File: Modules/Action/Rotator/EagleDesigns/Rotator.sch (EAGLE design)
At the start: 9 parts, among them U2 ATMEGA328P_TQFP

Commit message: Revert "Merge branch 'version-1.2'"
This reverts commit 982d9c85d5bd00c48b539e840003de48d3cf178d, reversing
changes made to b3895ae538c161df72313035d3e956c7a5ec4dbc.
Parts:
- removed C1, C2: 22pF, adafruit:C-USC0603
- removed R2: 10K, resistor:R-US_R0603
- removed U$2: NX503, MakerWear:NX503
- removed U2: ATMEGA328P_TQFP, SparkFun-DigitalIC:ATMEGA328P_TQFP
- added U1: TINY85-20-DIP, SparkFun-DigitalIC:ATTINY45TINY85-20-DIP
- JP2: device SparkFun-Connectors:M03PTH -> SparkFun-Connectors:M04PTH
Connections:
- removed net 1X3SIN: U2.PC0(ADC0)
- removed net N$1: C1.1, U$2.P$1, U2.PB6(XTAL1/TOSC1)
- removed net N$3: C2.1, U$2.P$2, U2.PB7(XTAL2/TOSC2)
- removed net RESET: JP2.1, R2.1, U2.PC6(/RESET)
- removed net RX: JP2.2, U2.PD0(RXD)
- removed net TX: JP2.3, U2.PD1(TXD)
- new net MOSI: JP2.2, U1.PB0(MOSI)
- new net NRES: JP2.1, U1.PB5(NRES)
- new net OUT(MISO): JP2.3, JP3.1, U1.PB1(MISO)
- new net SCK: JP2.4, U1.PB2(SCK/ADC1)
- net 1X3SIN-SOUT: now also U1.PB3(ADC3)
- net GND: now also U1.GND; no longer C1.2, C2.2, U2.AGND, U2.GND@3, U2.GND@5
- net VCC: now also U1.VCC; no longer R2.2, U2.AVCC, U2.VCC@4, U2.VCC@6
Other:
- moved on the sheet: JP1, JP3, R1

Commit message: added Rotator #30 eagle files
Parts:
- removed U1: TINY85-20-DIP, SparkFun-DigitalIC:ATTINY45TINY85-20-DIP
- added C1, C2: 22pF, adafruit:C-USC0603
- added R2: 10K, resistor:R-US_R0603
- added U$2: NX503, MakerWear:NX503
- added U2: ATMEGA328P_TQFP, SparkFun-DigitalIC:ATMEGA328P_TQFP
- JP2: device SparkFun-Connectors:M04PTH -> SparkFun-Connectors:M03PTH
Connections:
- removed net MOSI: JP2.2, U1.PB0(MOSI)
- removed net NRES: JP2.1, U1.PB5(NRES)
- removed net OUT(MISO): JP2.3, JP3.1, U1.PB1(MISO)
- removed net SCK: JP2.4, U1.PB2(SCK/ADC1)
- new net 1X3SIN: U2.PC0(ADC0)
- new net N$1: C1.1, U$2.P$1, U2.PB6(XTAL1/TOSC1)
- new net N$3: C2.1, U$2.P$2, U2.PB7(XTAL2/TOSC2)
- new net RESET: JP2.1, R2.1, U2.PC6(/RESET)
- new net RX: JP2.2, U2.PD0(RXD)
- new net TX: JP2.3, U2.PD1(TXD)
- net 1X3SIN-SOUT: no longer U1.PB3(ADC3)
- net GND: now also C1.2, C2.2, U2.AGND, U2.GND@3, U2.GND@5; no longer U1.GND
- net VCC: now also R2.2, U2.AVCC, U2.VCC@4, U2.VCC@6; no longer U1.VCC
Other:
- moved on the sheet: JP1, JP3, R1

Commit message: fixed eagle files for new modules
SIN/SOUT was not correctly connected in them.
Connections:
- removed net 1X3SIN: U2.PC0(ADC0)
- new net SERVO: JP3.1, U2.PB1(OC1A)
- net 1X3SIN-SOUT: now also U2.PC0(ADC0)
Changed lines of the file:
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@@
 <pinref part="R1" gate="G$1" pin="2"/>
+</segment>
+<segment>
+<pinref part="U2" gate="U$1" pin="PC0(ADC0)"/>
+<wire x1="208.28" y1="55.88" x2="228.6" y2="55.88" width="0.1524" layer="91"/>
+<junction x="228.6" y="55.88"/>
+<label x="210.82" y="55.88" size="1.778" layer="95"/>
 </segment>
 </net>
@@
 </segment>
 </net>
-<net name="1X3SIN" class="0">
-<segment>
-<pinref part="U2" gate="U$1" pin="PC0(ADC0)"/>
-<wire x1="208.28" y1="55.88" x2="220.98" y2="55.88" width="0.1524" layer="91"/>
-<junction x="220.98" y="55.88"/>
-<label x="210.82" y="55.88" size="1.778" layer="95"/>
-</segment>
-</net>
 <net name="N$1" class="0">
 <segment>
@@
 </segment>
 </net>
+<net name="SERVO" class="0">
+<segment>
+<pinref part="U2" gate="U$1" pin="PB1(OC1A)"/>
+<wire x1="208.28" y1="7.62" x2="220.98" y2="7.62" width="0.1524" layer="91"/>
+<junction x="220.98" y="7.62"/>
+<label x="210.82" y="7.62" size="1.778" layer="95"/>
+</segment>
+<segment>
+<pinref part="JP3" gate="G$1" pin="1"/>
+<wire x1="302.26" y1="30.48" x2="284.48" y2="30.48" width="0.1524" layer="91"/>
+<junction x="284.48" y="30.48"/>
+<label x="287.02" y="30.48" size="1.778" layer="95"/>
+</segment>
+</net>

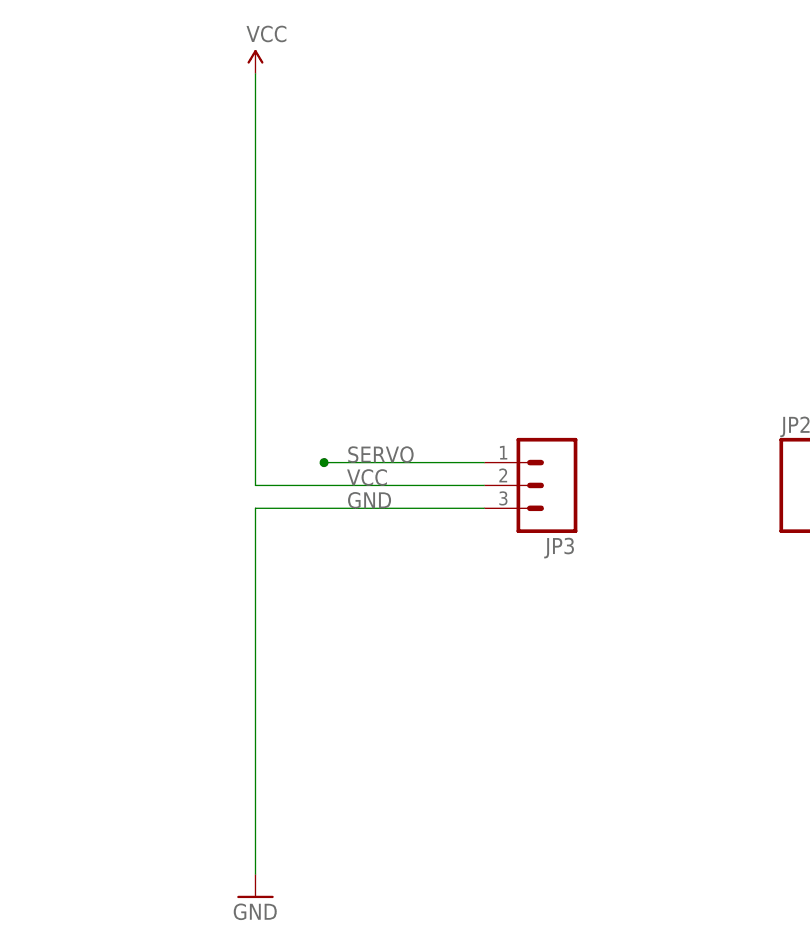
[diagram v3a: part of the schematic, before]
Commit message: Rotator: added final PCB #30
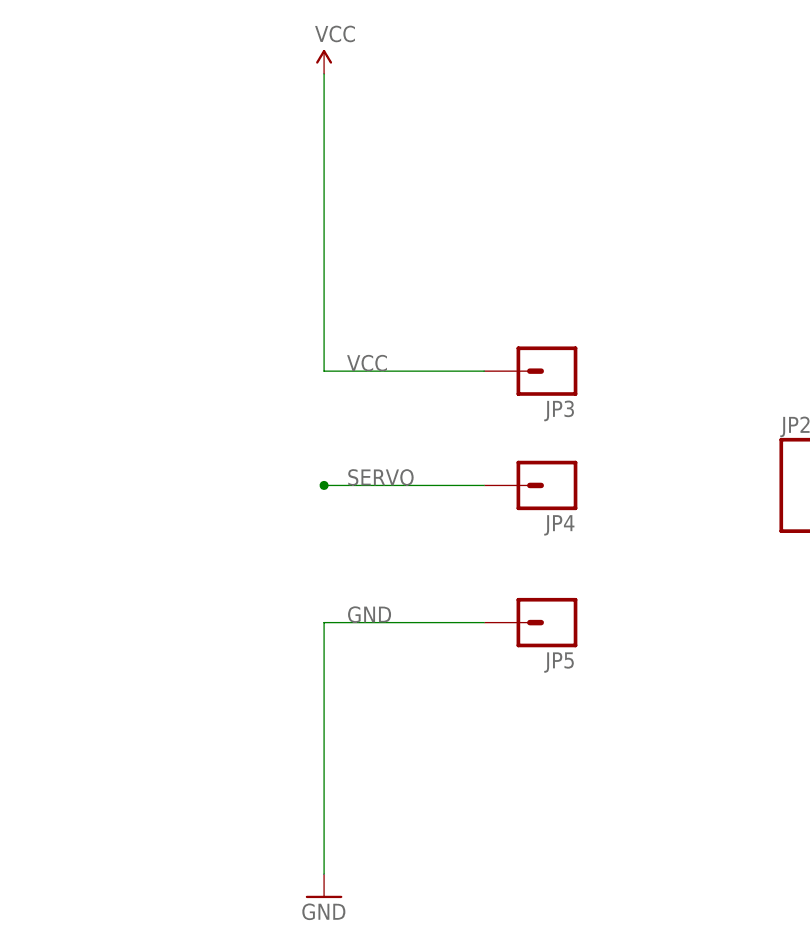
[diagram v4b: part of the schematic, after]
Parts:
- added JP4, JP5: (no value), SparkFun-Connectors:M01PTH
- JP3: device SparkFun-Connectors:M03PTH -> SparkFun-Connectors:M01PTH
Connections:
- net GND: now also JP5.1; no longer JP3.3
- net SERVO: now also JP4.1; no longer JP3.1
- net VCC: now also JP3.1; no longer JP3.2
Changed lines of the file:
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@@
 <part name="GND5" library="SparkFun-Aesthetics" deviceset="GND" device=""/>
 <part name="R1" library="adafruit" deviceset="R-US_" device="R0603" value="1M"/>
-<part name="JP3" library="SparkFun-Connectors" deviceset="M03" device="PTH"/>
 <part name="SUPPLY3" library="SparkFun-Aesthetics" deviceset="VCC" device=""/>
 <part name="GND3" library="SparkFun-Aesthetics" deviceset="GND" device=""/>
@@
 <part name="C1" library="adafruit" deviceset="C-US" device="C0603" value="22pF"/>
 <part name="C2" library="adafruit" deviceset="C-US" device="C0603" value="22pF"/>
+<part name="JP3" library="SparkFun-Connectors" deviceset="M01" device="PTH"/>
+<part name="JP4" library="SparkFun-Connectors" deviceset="M01" device="PTH"/>
+<part name="JP5" library="SparkFun-Connectors" deviceset="M01" device="PTH"/>
 </parts>
 <sheets>
@@
 <instance part="GND5" gate="1" x="58.42" y="-17.78"/>
 <instance part="R1" gate="G$1" x="58.42" y="15.24" rot="R90"/>
-<instance part="JP3" gate="G$1" x="309.88" y="27.94" rot="R180"/>
-<instance part="SUPPLY3" gate="G$1" x="276.86" y="73.66"/>
-<instance part="GND3" gate="1" x="276.86" y="-17.78"/>
+<instance part="SUPPLY3" gate="G$1" x="284.48" y="73.66"/>
+<instance part="GND3" gate="1" x="284.48" y="-17.78"/>
 <instance part="JP2" gate="G$1" x="337.82" y="27.94"/>
 <instance part="U2" gate="U$1" x="185.42" y="25.4"/>
@@
 <instance part="C1" gate="G$1" x="96.52" y="-10.16"/>
 <instance part="C2" gate="G$1" x="121.92" y="-10.16"/>
+<instance part="JP3" gate="G$1" x="309.88" y="40.64" rot="R180"/>
+<instance part="JP4" gate="G$1" x="309.88" y="27.94" rot="R180"/>
+<instance part="JP5" gate="G$1" x="309.88" y="12.7" rot="R180"/>
 </instances>
 <busses>
@@
 </segment>
 <segment>
-<pinref part="JP3" gate="G$1" pin="2"/>
-<wire x1="302.26" y1="27.94" x2="276.86" y2="27.94" width="0.1524" layer="91"/>
-<wire x1="276.86" y1="27.94" x2="276.86" y2="73.66" width="0.1524" layer="91"/>
 <pinref part="SUPPLY3" gate="G$1" pin="VCC"/>
-<label x="287.02" y="27.94" size="1.778" layer="95"/>
+<pinref part="JP3" gate="G$1" pin="1"/>
+<wire x1="284.48" y1="40.64" x2="284.48" y2="73.66" width="0.1524" layer="91"/>
+<wire x1="302.26" y1="40.64" x2="284.48" y2="40.64" width="0.1524" layer="91"/>
+<label x="287.02" y="40.64" size="1.778" layer="95"/>
 </segment>
 <segment>
@@
 </segment>
 <segment>
-<pinref part="JP3" gate="G$1" pin="3"/>
-<wire x1="302.26" y1="25.4" x2="276.86" y2="25.4" width="0.1524" layer="91"/>
-<wire x1="276.86" y1="25.4" x2="276.86" y2="-15.24" width="0.1524" layer="91"/>
+<wire x1="284.48" y1="12.7" x2="284.48" y2="-15.24" width="0.1524" layer="91"/>
 <pinref part="GND3" gate="1" pin="GND"/>
-<label x="287.02" y="25.4" size="1.778" layer="95"/>
+<pinref part="JP5" gate="G$1" pin="1"/>
+<wire x1="302.26" y1="12.7" x2="284.48" y2="12.7" width="0.1524" layer="91"/>
+<label x="287.02" y="12.7" size="1.778" layer="95"/>
 </segment>
 <segment>
@@
 <net name="SERVO" class="0">
 <segment>
+<pinref part="JP4" gate="G$1" pin="1"/>
+<wire x1="302.26" y1="27.94" x2="284.48" y2="27.94" width="0.1524" layer="91"/>
+<junction x="284.48" y="27.94"/>
+<label x="287.02" y="27.94" size="1.778" layer="95"/>
+</segment>
+<segment>
 <pinref part="U2" gate="U$1" pin="PB1(OC1A)"/>
 <wire x1="208.28" y1="7.62" x2="220.98" y2="7.62" width="0.1524" layer="91"/>
@@
 <label x="210.82" y="7.62" size="1.778" layer="95"/>
 </segment>
-<segment>
-<pinref part="JP3" gate="G$1" pin="1"/>
-<wire x1="302.26" y1="30.48" x2="284.48" y2="30.48" width="0.1524" layer="91"/>
-<junction x="284.48" y="30.48"/>
-<label x="287.02" y="30.48" size="1.778" layer="95"/>
-</segment>
-</net>
+</net>

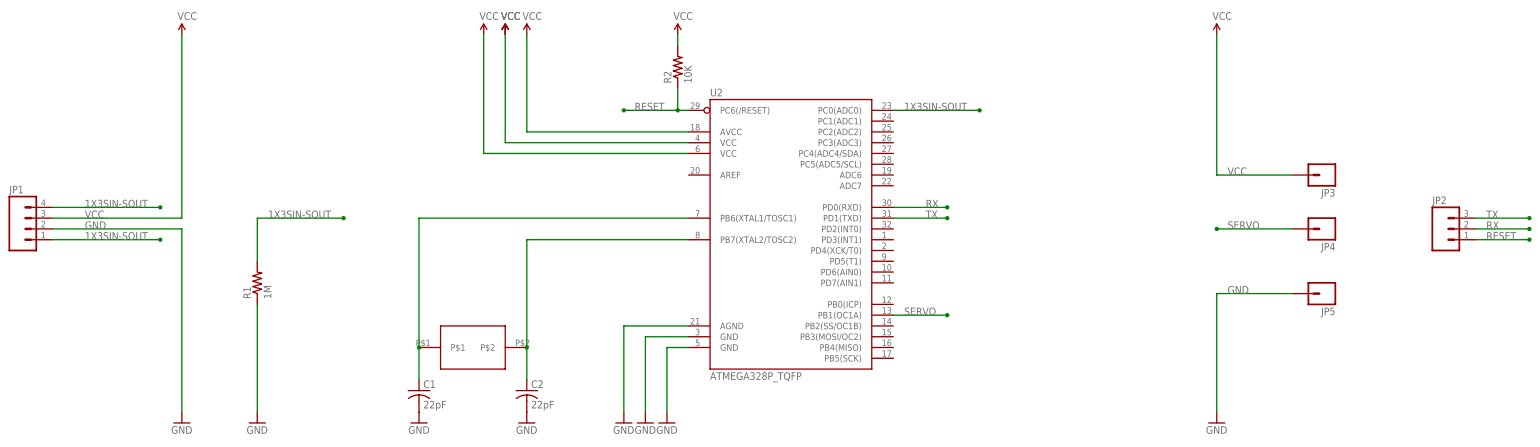
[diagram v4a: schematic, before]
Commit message: Rotator: removed crystal, modified to work with new bootloader #30
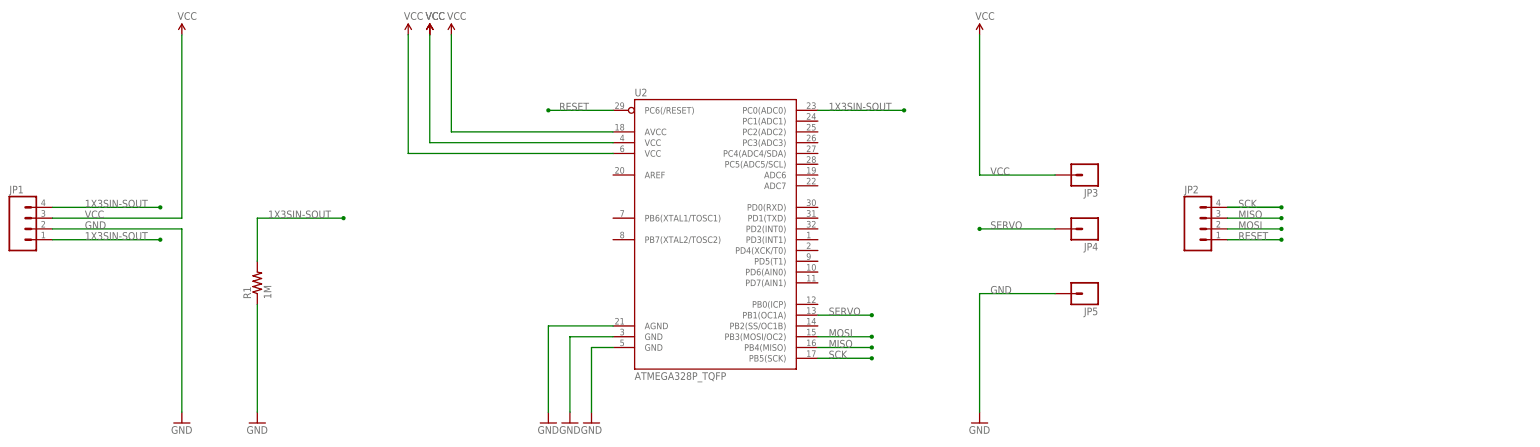
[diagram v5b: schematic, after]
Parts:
- removed C1, C2: 22pF, adafruit:C-USC0603
- removed R2: 10K, resistor:R-US_R0603
- removed U$2: NX503, MakerWear:NX503
- JP2: device SparkFun-Connectors:M03PTH -> SparkFun-Connectors:M04PTH
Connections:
- removed net N$1: C1.1, U$2.P$1, U2.PB6(XTAL1/TOSC1)
- removed net N$3: C2.1, U$2.P$2, U2.PB7(XTAL2/TOSC2)
- removed net RX: JP2.2, U2.PD0(RXD)
- removed net TX: JP2.3, U2.PD1(TXD)
- new net MISO: JP2.3, U2.PB4(MISO)
- new net MOSI: JP2.2, U2.PB3(MOSI/OC2)
- new net SCK: JP2.4, U2.PB5(SCK)
- net GND: no longer C1.2, C2.2
- net RESET: no longer R2.1
- net VCC: no longer R2.2
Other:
- moved on the sheet: JP3, JP4, JP5, U2
